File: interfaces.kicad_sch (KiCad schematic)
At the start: 92 parts, among them IC3 TPD8S009DSMR, J6 685119134923, J7 693071020811, J9 USB4105-GF-A, Q1 BSS138APW, Q10 BSS138APW, Q2 BSS138APW, Q3 BSS138APW, Q4 BSS138APW, Q5 BSS138APW, Q6 BSS138APW, Q9 BSS138APW, U7 FT4232H-56Q, Y2 ABM8G-12.000MHZ-18-D2Y-T

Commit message: Rebase to Rev. 1.2.2
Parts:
- removed C10, C226: C_1u_0402, antmicro-footprints:0402-cap, symbol antmicroCapacitors0402:C_1u_0402
- removed C184, C185, C186, C188, C191, C192, C196, C197, C252, C311: C_100n_0402, antmicro-footprints:0402-cap, symbol antmicroCapacitors0402:C_100n_0402
- removed C187, C189, C195: C_4u7_0402, data-center-dram-tester-footprints:0402-cap, symbol data-center-dram-tester:C_4u7_0402
- removed C190, C193: C_18p_0402, data-center-dram-tester-footprints:0402-cap, symbol data-center-dram-tester:C_18p_0402
- removed D17: APTF1616SURKCGKSYKC, antmicro-footprints:KPTF1616RGBC11, symbol antmicroLEDIndicationDiscrete:APTF1616SURKCGKSYKC
- removed D3: TPD2E009, data-center-dram-tester-footprints:SOT-3, symbol data-center-dram-tester:TPD2E009
- removed D5, D6, D7, D8, D9: KP-1608CGCK, data-center-dram-tester-footprints:LED_0603, symbol data-center-dram-tester:KP-1608CGCK
- removed FB4, FB5: BLM18AG601SN1D, data-center-dram-tester-footprints:0603, symbol data-center-dram-tester:BLM18AG601SN1D
- removed IC3: TPD8S009DSMR, data-center-dram-tester-footprints:R-PDSO-N15, symbol data-center-dram-tester:TPD8S009DSMR
- removed J6: 685119134923, data-center-dram-tester-footprints:HDMI_A_Female_685119134923, symbol data-center-dram-tester:685119134923
- removed J7: 693071020811, antmicro-footprints:WE_693071020811, symbol antmicroMemoryConnectorsPCCardSockets:693071020811
- removed J9: USB4105-GF-A, antmicro-footprints:GCT_USB4105-GF-A, symbol antmicroUSBDVIHDMIConnectors:USB4105-GF-A
- removed Q1, Q10, Q2, Q3, Q4, Q5, Q6, Q9: BSS138APW, data-center-dram-tester-footprints:SC70-3, symbol data-center-dram-tester:BSS138APW
- removed R1, R18, R19, R2, R20, R25, R3, R37, R4, R5, R6, R7, R8: R_22R_0402, data-center-dram-tester-footprints:0402-res, symbol data-center-dram-tester:R_22R_0402
- removed R125, R147, R187, R188, R189, R50, R51, R52, R53, R54: R_330R_0402, data-center-dram-tester-footprints:0402-res, symbol data-center-dram-tester:R_330R_0402
- removed R129: R_12k_0402, data-center-dram-tester-footprints:0402-res, symbol data-center-dram-tester:R_12k_0402
- removed R130: R_10k_0402, data-center-dram-tester-footprints:0402-res, symbol data-center-dram-tester:R_10k_0402
- removed R131, R132, R133, R134, R135, R137, R138: R_20k_0402, data-center-dram-tester-footprints:0402-res, symbol data-center-dram-tester:R_20k_0402
- removed R136: R_220R_0402, data-center-dram-tester-footprints:0402-res, symbol data-center-dram-tester:R_220R_0402
- removed R139, R140, R141, R142, R143, R144, R145, R146: R_0R_0402, data-center-dram-tester-footprints:0402-res, symbol data-center-dram-tester:R_0R_0402
- removed R15, R16: R_5k11_0402, antmicro-footprints:0402-res, symbol antmicroResistors0402:R_5k11_0402
- removed R190: R_4k7_0402, data-center-dram-tester-footprints:0402-res, symbol data-center-dram-tester:R_4k7_0402
- removed S1: 1-1825027-1, antmicro-footprints:TE_1-1825027-1, symbol antmicroTactileSwitches:1-1825027-1
- removed TP1, TP11, TP2, TP3, TP4, TP5, VBUS1: TP_SMD1MM, data-center-dram-tester-footprints:Testpoint_smd_1mm, symbol data-center-dram-tester:TP_SMD1MM
- removed U7: FT4232H-56Q, antmicro-footprints:QFN-56-1EP_8x8mm_P0.5mm_EP5.5.9x5.9mm, symbol antmicroInterfaceControllers:FT4232H-56Q
- removed Y2: ABM8G-12.000MHZ-18-D2Y-T, data-center-dram-tester-footprints:KX-7, symbol data-center-dram-tester:ABM8G-12.000MHZ-18-D2Y-T
- added C10, C226: C_1u_0402, data-center-rdimm-ddr4-tester-footprints:C_0402_1005Metric, symbol data-center-rdimm-ddr4-tester:C_1u_0402
- added C184, C185, C186, C188, C191, C192, C196, C197, C252, C311: C_100n_0402, data-center-rdimm-ddr4-tester-footprints:C_0402_1005Metric, symbol data-center-rdimm-ddr4-tester:C_100n_0402
- added C187, C189, C195: C_4u7_0402, data-center-rdimm-ddr4-tester-footprints:C_0402_1005Metric, symbol data-center-rdimm-ddr4-tester:C_4u7_0402
- added C190, C193: C_18p_0402, data-center-rdimm-ddr4-tester-footprints:C_0402_1005Metric, symbol data-center-rdimm-ddr4-tester:C_18p_0402
- added D17: LED_RGY_0606_APTF1616SURKCGKSYKC, data-center-rdimm-ddr4-tester-footprints:LED_RGY_1.6x1.6mm_APTF1616, symbol data-center-rdimm-ddr4-tester:LED_RGY_0606_APTF1616SURKCGKSYKC
- added D3: TPD2E009_SOT-9X3, data-center-rdimm-ddr4-tester-footprints:SOT-723, symbol data-center-rdimm-ddr4-tester:TPD2E009_SOT-9X3
- added D5, D6, D7, D8, D9: LED_G_0603_KP-1608CGCK, data-center-rdimm-ddr4-tester-footprints:LED_0603_1608Metric_G, symbol data-center-rdimm-ddr4-tester:LED_G_0603_KP-1608CGCK
- added FB4, FB5: FB_600Z_0.5A_0603, data-center-rdimm-ddr4-tester-footprints:FB_0603_1608Metric, symbol data-center-rdimm-ddr4-tester:FB_600Z_0.5A_0603
- added IC3: TPD8S009DSMR, data-center-rdimm-ddr4-tester-footprints:R-PDSO-N15, symbol data-center-rdimm-ddr4-tester:TPD8S009DSMR
- added J6: HDMI_A_Female_685119134923, data-center-rdimm-ddr4-tester-footprints:HDMI-A_Wurth_685119134923, symbol data-center-rdimm-ddr4-tester:HDMI_A_Female_685119134923
- added J7: MicroSD_693071020811, data-center-rdimm-ddr4-tester-footprints:MicroSD_Wurth_693071020811, symbol data-center-rdimm-ddr4-tester:MicroSD_693071020811
- added J9: USB-C_USB4105-GF-A, data-center-rdimm-ddr4-tester-footprints:USB-C_GCT_USB4105-GF-A, symbol data-center-rdimm-ddr4-tester:USB-C_USB4105-GF-A
- added Q1, Q10, Q2, Q3, Q4, Q5, Q6, Q9: BSS138PW, data-center-rdimm-ddr4-tester-footprints:SC70-3, symbol data-center-rdimm-ddr4-tester:BSS138PW
- added R1, R18, R19, R2, R20, R25, R3, R37, R4, R5, R6, R7, R8: R_22R_0402, data-center-rdimm-ddr4-tester-footprints:R_0402_1005Metric, symbol data-center-rdimm-ddr4-tester:R_22R_0402
- added R125, R147, R187, R188, R189, R50, R51, R52, R53, R54: R_330R_0402, data-center-rdimm-ddr4-tester-footprints:R_0402_1005Metric, symbol data-center-rdimm-ddr4-tester:R_330R_0402
- added R129: R_12k_0402, data-center-rdimm-ddr4-tester-footprints:R_0402_1005Metric, symbol data-center-rdimm-ddr4-tester:R_12k_0402
- added R130: R_10k_0402, data-center-rdimm-ddr4-tester-footprints:R_0402_1005Metric, symbol data-center-rdimm-ddr4-tester:R_10k_0402
- added R131, R132, R133, R134, R135, R137, R138: R_20k_0402, data-center-rdimm-ddr4-tester-footprints:R_0402_1005Metric, symbol data-center-rdimm-ddr4-tester:R_20k_0402
- added R136: R_220R_0402, data-center-rdimm-ddr4-tester-footprints:R_0402_1005Metric, symbol data-center-rdimm-ddr4-tester:R_220R_0402
- added R139, R140, R141, R142, R143, R144, R145, R146: R_0R_0402, data-center-rdimm-ddr4-tester-footprints:R_0402_1005Metric, symbol data-center-rdimm-ddr4-tester:R_0R_0402
- added R15, R16: R_5k11_0402, data-center-rdimm-ddr4-tester-footprints:R_0402_1005Metric, symbol data-center-rdimm-ddr4-tester:R_5k11_0402
- added R190: R_4k7_0402, data-center-rdimm-ddr4-tester-footprints:R_0402_1005Metric, symbol data-center-rdimm-ddr4-tester:R_4k7_0402
- added S1: SW_1-1825027-1, data-center-rdimm-ddr4-tester-footprints:SW_Tactile_SPST_Angled_TE_1825027, symbol data-center-rdimm-ddr4-tester:SW_1-1825027-1
- added TP1, TP11, TP2, TP3, TP4, TP5, VBUS1: TP_1mm_SMD, data-center-rdimm-ddr4-tester-footprints:Testpoint_smd_1mm, symbol data-center-rdimm-ddr4-tester:TP_1mm_SMD
- added U7: FT4232H_VQFN, data-center-rdimm-ddr4-tester-footprints:QFN-56-1EP_8x8mm_P0.5mm, symbol data-center-rdimm-ddr4-tester:FT4232H_VQFN
- added Y2: Oscillator_SMD_12MHz_KX-7, data-center-rdimm-ddr4-tester-footprints:Oscillator_SMD_Geyer_KX-7-4Pin_3.2x2.5mm, symbol data-center-rdimm-ddr4-tester:Oscillator_SMD_12MHz_KX-7
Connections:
- net 1V8_FT: now also C195.1, C196.1, C197.1, U7.2 (V_{CORE}), U7.31 (V_{CORE}), U7.43 (V_{REGOUT})
- net 3V3_SYS: now also C10.1, C186.1, C188.1, C191.1, C192.1, D17.1 (A), D5.1, D6.1, D7.1, D8.1, D9.1, FB4.1, FB5.1, IC3.13 (VCC), IC3.15 (VCC), J7.4 (VDD), R130.1, R131.1, R132.1, R133.1, R134.1, R135.1, R137.1, R138.1, R190.1, U7.16 (V_{CCIO}), U7.36 (V_{CCIO}), U7.44 (V_{REGIN}), U7.50 (V_{CCIO})
- net AUX_JTAG_RST: now also R5.2
- net AUX_JTAG_TCK: now also R1.2
- net AUX_JTAG_TDI: now also R2.2
- net AUX_JTAG_TDO: now also R3.2
- net AUX_JTAG_TMS: now also R4.2
- net C_TMDS_CLK_N: now also IC3.12 (D3-), J6.12, R139.2
- net C_TMDS_CLK_P: now also IC3.10 (D3+), J6.10, R140.2
- net C_TMDS_D0_N: now also IC3.9 (D2-), J6.9, R141.2
- net C_TMDS_D0_P: now also IC3.7 (D2+), J6.7, R142.2
- net C_TMDS_D1_N: now also IC3.6 (D1-), J6.6, R143.2
- net C_TMDS_D1_P: now also IC3.4 (D1+), J6.4, R144.2
- net C_TMDS_D2_N: now also IC3.3 (D0-), J6.3, R145.2
- net C_TMDS_D2_P: now also IC3.1 (D0+), J6.1, R146.2
- net DBG_USB_N: now also D3.1, J9.A7 (D-), J9.B7 (D-), U7.7 (D-)
- net DBG_USB_P: now also D3.2, J9.A6 (D+), J9.B6 (D+), U7.8 (D+)
- net GND: now also C10.2, C184.2, C185.2, C186.2, C187.2, C188.2, C189.2, C190.2, C191.2, C192.2, C193.2, C195.2, C196.2, C197.2, C226.2, C252.2, C311.2, D3.3, IC3.11 (GND), IC3.2 (GND), IC3.5 (GND), IC3.8 (GND), J6.11, J6.17, J6.2, J6.5, J6.8, J7.6 (VSS), J7.SH, J9.A1 (GND), J9.A12 (GND), J9.B1 (GND), J9.B12 (GND), Q1.2 (S), Q10.2 (S), Q2.2 (S), Q3.2 (S), Q4.2 (S), Q5.2 (S), Q6.2 (S), Q9.2 (S), R125.1, R129.1, R147.1, R15.1, R16.2, S1.2, S1.SH, U7.10 (TEST), U7.21 (GND), U7.41 (GND), U7.45 (GND), U7.57 (GND), Y2.2 (SH), Y2.4 (SH)
- net GND1: now also C311.1, J6.SH, R147.2
- net GNDS: now also C252.1, J9.SH (SHIELD), R125.2
- net HOT_SWAP_BUTTON: now also C226.1, R190.2, S1.1
- net HOT_SWAP_GREEN: now also Q9.1 (G)
- net HOT_SWAP_RED: now also Q10.1 (G)
- net HOT_SWAP_YELLOW: now also Q1.1 (G)
- net SD_CD: now also R131.2, R136.1
- net SD_CLK: now also J7.5 (CLK), R134.2
- net SD_CMD: now also J7.3 (CMD), R135.2
- net SD_DAT0: now also J7.7 (DAT0), R133.2
- net SD_DAT1: now also J7.8 (DAT1), R132.2
- net SD_DAT2: now also J7.1 (DAT2), R138.2
- net SD_DAT3: now also J7.2 (DAT3/CD), R137.2
- net TCK_JTAG: now also R18.2
- net TDI_JTAG: now also R19.2
- net TDO_JTAG: now also R20.2
- net TMDS_CLK_N: now also R139.1
- net TMDS_CLK_P: now also R140.1
- net TMDS_D0_N: now also R141.1
- net TMDS_D0_P: now also R142.1
- net TMDS_D1_N: now also R143.1
- net TMDS_D1_P: now also R144.1
- net TMDS_D2_N: now also R145.1
- net TMDS_D2_P: now also R146.1
- net TMS_JTAG: now also R25.2
- net UART0_RX: now also R6.2
- net UART0_TX: now also R7.2
- net UART1_RX: now also R8.2
- net UART1_TX: now also R37.2
- net USR_LED1: now also Q2.1 (G)
- net USR_LED2: now also Q4.1 (G)
- net USR_LED3: now also Q3.1 (G)
- net USR_LED4: now also Q5.1 (G)
- net USR_LED5: now also Q6.1 (G)
- net VBUS: now also J9.A4 (VBUS), J9.A9 (VBUS), J9.B4 (VBUS), J9.B9 (VBUS), VBUS1.1
- new net: R1.1, U7.22 (BDBUS0)
- new net: R2.1, U7.23 (BDBUS1)
- new net: R3.1, U7.24 (BDBUS2)
- new net: R4.1, U7.25 (BDBUS3)
- new net: R6.1, U7.32 (CDBUS0)
- new net: R37.1, U7.46 (DDBUS1)
- new net: R7.1, U7.33 (CDBUS1)
- new net: R8.1, U7.42 (DDBUS0)
- new net: D5.2, R50.1
- new net: Q2.3 (D), R50.2
- new net: C185.1, C189.1, FB5.2, U7.5 (V_{PHY})
- new net: C184.1, C187.1, FB4.2, U7.9 (V_{PLL})
- new net: R129.2, U7.6 (REF)
- new net: R130.2, U7.11 (~{RESET})
- new net: C190.1, U7.3 (OSCI), Y2.1
- new net: C193.1, U7.4 (OSCO), Y2.3
- new net: D7.2, R52.1
- new net: Q4.3 (D), R52.2
- new net: D8.2, R53.1
- new net: Q5.3 (D), R53.2
- new net: D9.2, R54.1
- new net: Q6.3 (D), R54.2
- new net: D6.2, R51.1
- new net: Q3.3 (D), R51.2
- new net: R5.1, U7.27 (BDBUS5)
- new net: J6.13, TP1.1
- new net: J6.15, TP2.1
- new net: J6.16, TP4.1
- new net: J6.18, TP5.1
- new net: J6.19, TP3.1
- new net: R18.1, U7.12 (ADBUS0)
- new net: R19.1, U7.13 (ADBUS1)
- new net: R20.1, U7.14 (ADBUS2)
- new net: R25.1, U7.15 (ADBUS3)
- new net: J7.9 (CD_SW1), R136.2
- new net: TP11.1, U7.18 (ADBUS5)
- new net: J9.A5 (CC1), R15.2
- new net: Q9.3 (D), R188.2
- new net: J9.B5 (CC2), R16.1
- new net: D17.4 (C_{Y}), R187.1
- new net: Q1.3 (D), R187.2
- new net: D17.2 (C_{R}), R189.1
- new net: Q10.3 (D), R189.2
- new net: D17.3 (C_{G}), R188.1
- no-connect marks 9 -> 26

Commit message: Update designators and sync schematic with PCB
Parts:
- renumbered C184 to C6001, C190 to C6002, C185 to C6003, C187 to C6004, C186 to C6005, C189 to C6006, C193 to C6007, C188 to C6008, C191 to C6009, C192 to C6010, C195 to C6011, C196 to C6012, C197 to C6013, C226 to C6014, C10 to C6015, C252 to C6016, C311 to C6017, D5 to D6001, D6 to D6002, D7 to D6003, D8 to D6004, D9 to D6005, D17 to D6006, D3 to D6007, FB4 to FB6001, FB5 to FB6002, IC3 to IC6001, J6 to J6001, J9 to J6002, J7 to J6003, Q2 to Q6001, Q3 to Q6002, Q4 to Q6003, Q5 to Q6004, Q6 to Q6005, Q1 to Q6006, Q9 to Q6007, Q10 to Q6008, R50 to R6001, R51 to R6002, R52 to R6003, R130 to R6004, R129 to R6005, R53 to R6006, R54 to R6007, R18 to R6008, R19 to R6009, R20 to R6010, R25 to R6011, R1 to R6012, R2 to R6013, R3 to R6014, R4 to R6015, R5 to R6016, R6 to R6017, R7 to R6018, R8 to R6019, R37 to R6020, R187 to R6021, R188 to R6022, R189 to R6023, R15 to R6024, R16 to R6025, R190 to R6026, R139 to R6027, R140 to R6028, R141 to R6029, R142 to R6030, R131 to R6031, R143 to R6032, R132 to R6033, R133 to R6034, R144 to R6035, R134 to R6036, R136 to R6037, R145 to R6038, R135 to R6039, R137 to R6040, R146 to R6041, R138 to R6042, R125 to R6043, R147 to R6044, S1 to S6001, TP11 to TP6001, TP1 to TP6002, TP2 to TP6003, TP3 to TP6004, TP4 to TP6005, TP5 to TP6006, U7 to U6001, VBUS1 to VBUS6001, Y2 to Y6001

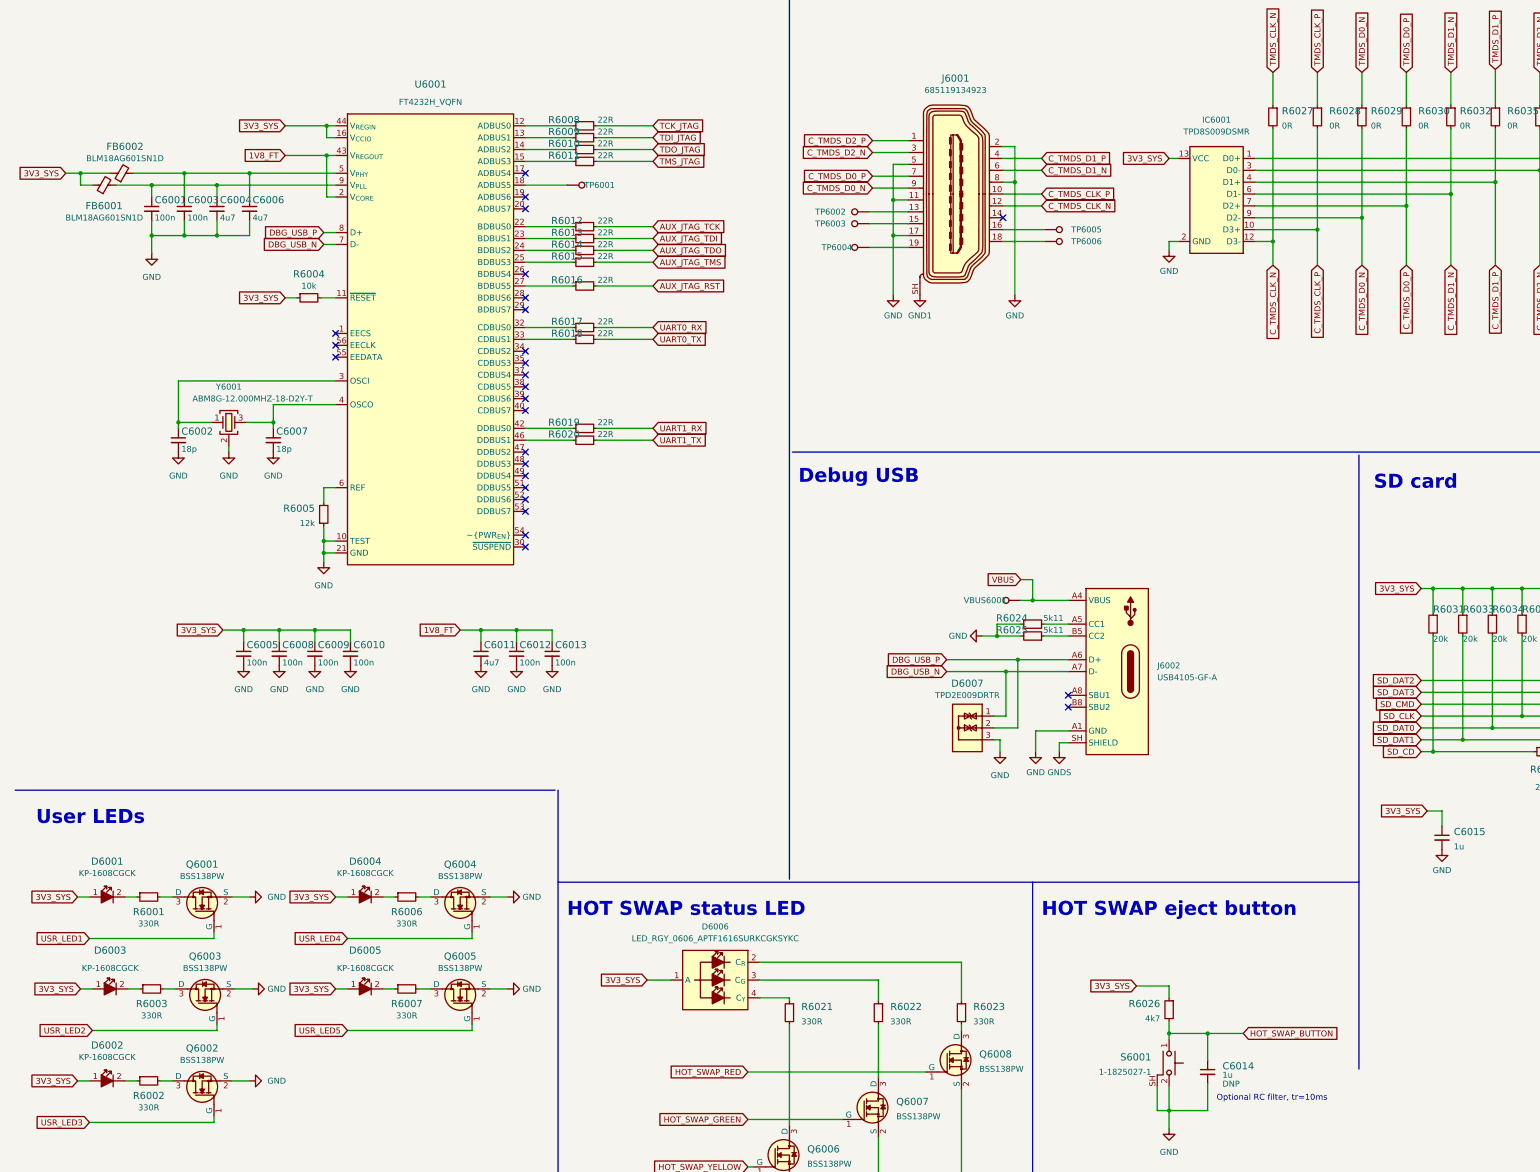
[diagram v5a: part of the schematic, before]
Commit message: Replace supply labels with proper symbols
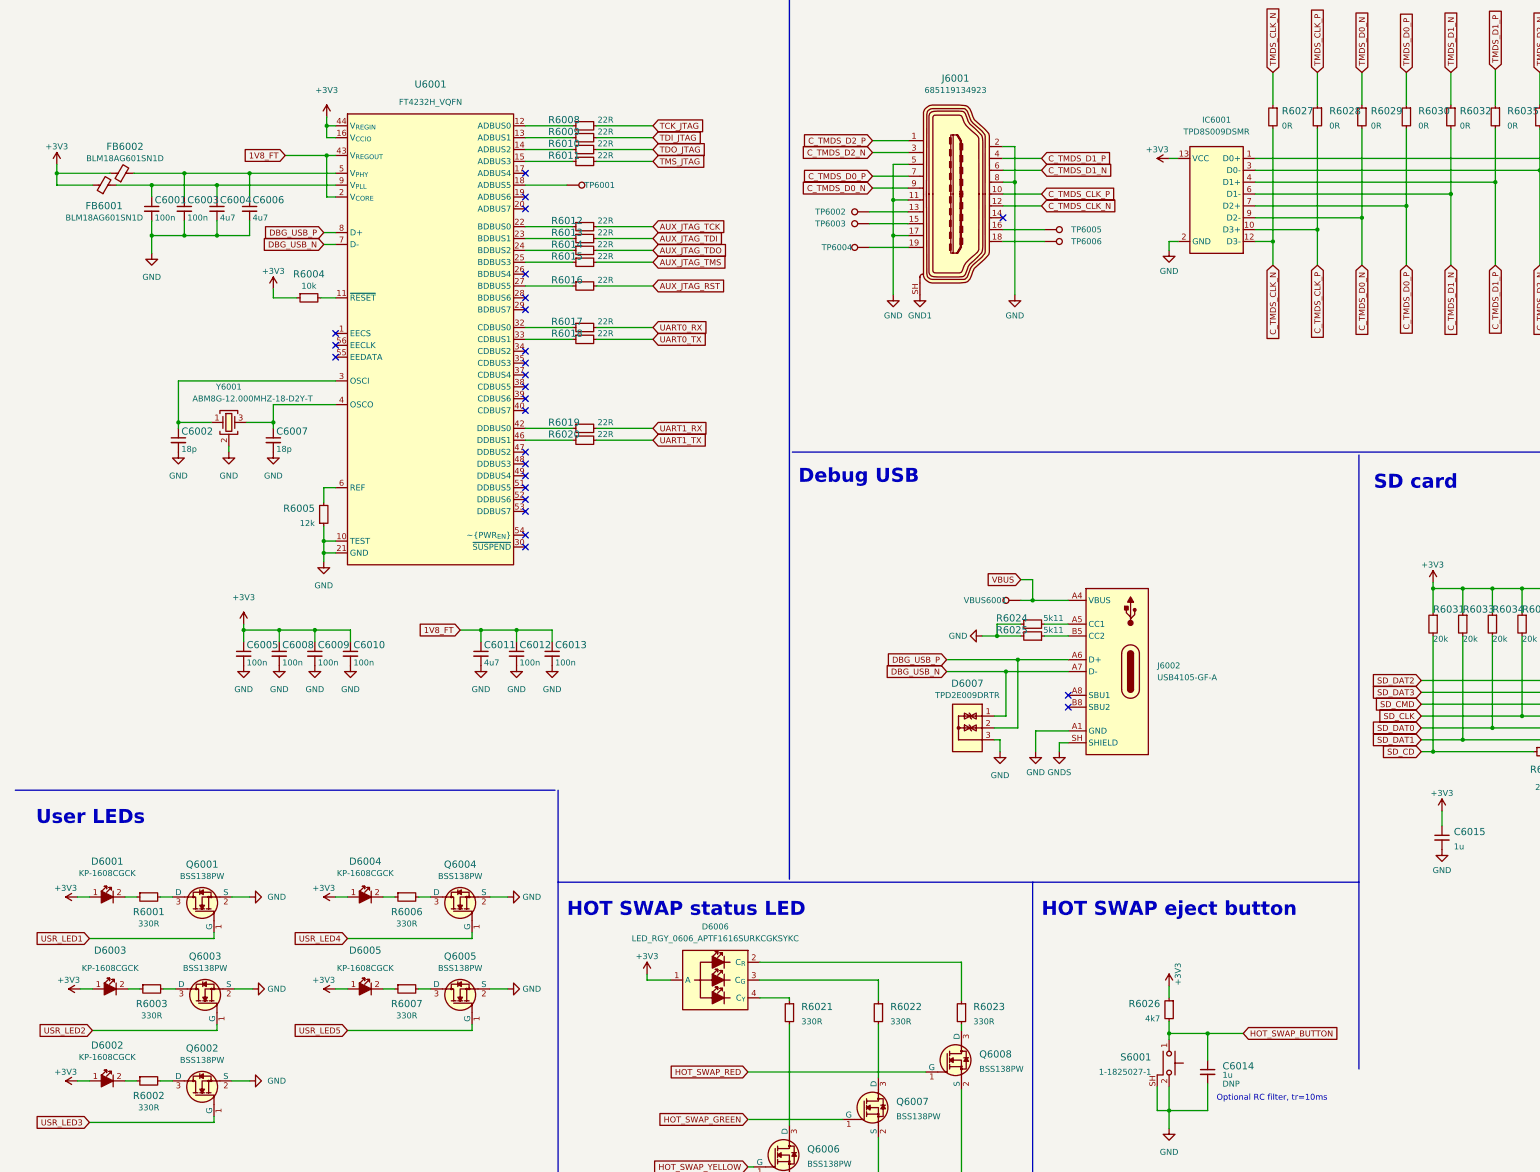
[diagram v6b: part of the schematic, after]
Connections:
- net 3V3_SYS renamed +3V3
